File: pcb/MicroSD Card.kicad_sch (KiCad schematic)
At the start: 2 parts, among them J4 Micro_SD_Card

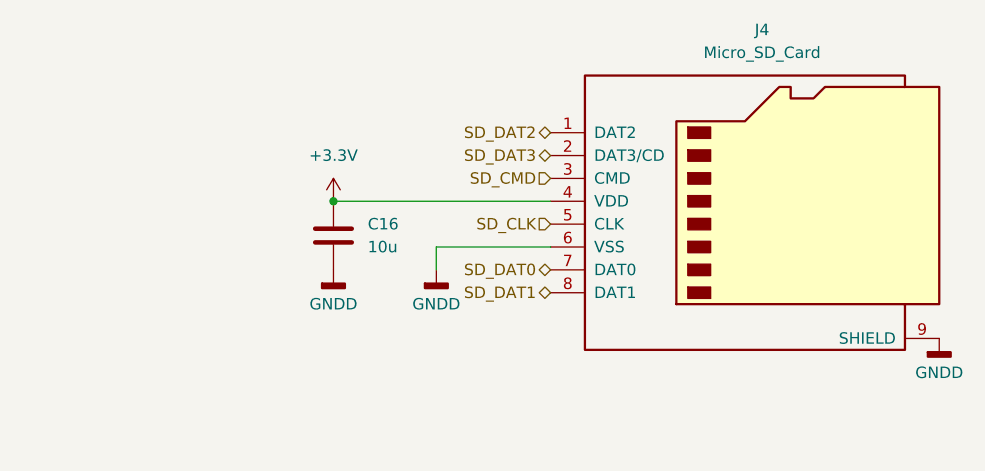
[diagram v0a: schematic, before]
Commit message: Updated Control Module Test bed schematics
Added Test points for Pyro controllers, Micro SD, and USB-C

Connected VDDUSB to 3.3V and not Vusb
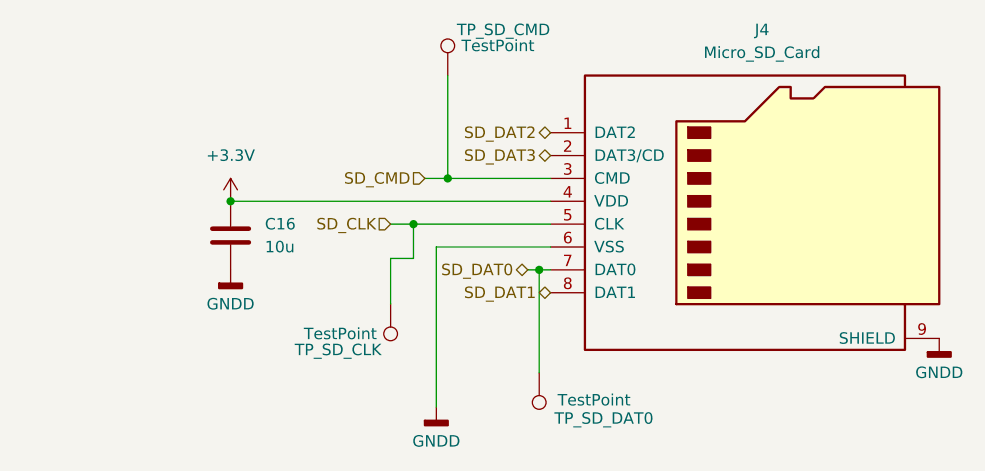
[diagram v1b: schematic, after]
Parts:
- added TP_SD_CLK, TP_SD_CMD, TP_SD_DAT0: TestPoint, TestPoint:TestPoint_Loop_D2.54mm_Drill1.5mm_Beaded, symbol Connector:TestPoint
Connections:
- net SD_CLK: now also TP_SD_CLK.1
- net SD_CMD: now also TP_SD_CMD.1
- net SD_DAT0: now also TP_SD_DAT0.1
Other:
- moved on the sheet: C16

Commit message: Added more testpoints
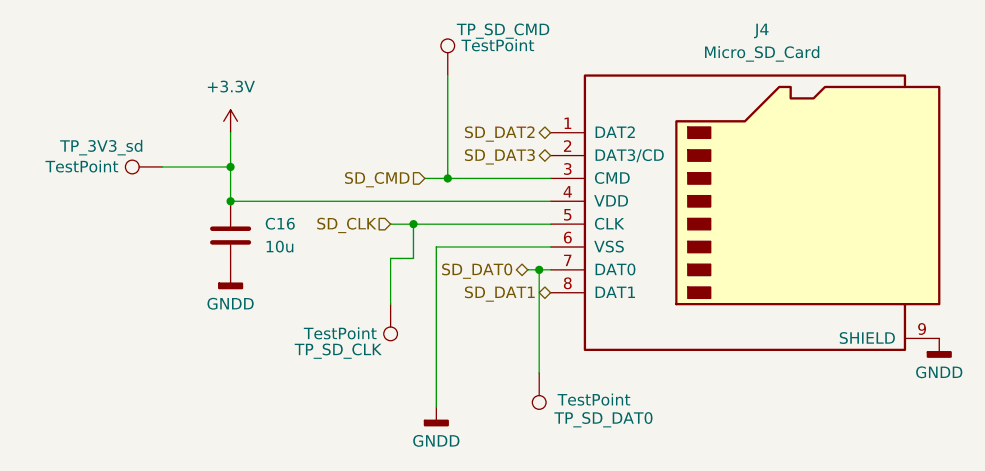
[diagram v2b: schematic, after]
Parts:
- added TP_3V3_sd: TestPoint, TestPoint:TestPoint_Loop_D2.54mm_Drill1.5mm_Beaded, symbol Connector:TestPoint
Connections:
- net +3.3V: now also TP_3V3_sd.1
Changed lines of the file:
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@@
+	)
+	(junction
+		(at 90.17 83.82)
+		(diameter 0)
+		(color 0 0 0 0)
 	)
 	(junction
@@
 	(wire
 		(pts
+			(xy 82.55 83.82) (xy 90.17 83.82)
+		)
+		(stroke
+			(width 0)
+			(type default)
+		)
+	)
+	(wire
+		(pts
 			(xy 110.49 90.17) (xy 125.73 90.17)
 		)
@@
 		(pts
 			(xy 124.46 95.25) (xy 124.46 106.68)
+		)
+		(stroke
+			(width 0)
+			(type default)
+		)
+	)
+	(wire
+		(pts
+			(xy 90.17 83.82) (xy 90.17 87.63)
+		)
+		(stroke
+			(width 0)
+			(type default)
+		)
+	)
+	(wire
+		(pts
+			(xy 90.17 80.01) (xy 90.17 83.82)
 		)
 		(stroke
@@
 	(symbol
 		(lib_id "power:+3.3V")
-		(at 90.17 87.63 0)
+		(at 90.17 80.01 0)
 		(unit 1)
 		(exclude_from_sim no)
@@
 		(fields_autoplaced yes)
 		(property "Reference" "#PWR050"
-			(at 90.17 91.44 0)
+			(at 90.17 83.82 0)
 			(effects
 				(font
@@
 		)
 		(property "Value" "+3.3V"
-			(at 90.17 82.55 0)
+			(at 90.17 74.93 0)
 			(effects
 				(font
@@
 		)
 		(property "Footprint" ""
-			(at 90.17 87.63 0)
+			(at 90.17 80.01 0)
 			(effects
 				(font
@@
 		)
 		(property "Datasheet" ""
-			(at 90.17 87.63 0)
+			(at 90.17 80.01 0)
 			(effects
 				(font
@@
 		)
 		(property "Description" "Power symbol creates a global label with name \"+3.3V\""
-			(at 90.17 87.63 0)
+			(at 90.17 80.01 0)
 			(effects
 				(font
@@
 					(unit 1)
 				)
+			)
+		)
+	)
+	(symbol
+		(lib_id "Connector:TestPoint")
+		(at 82.55 83.82 90)
+		(unit 1)
+		(exclude_from_sim no)
+		(in_bom yes)
+		(on_board yes)
+		(dnp no)
+		(property "Reference" "TP_3V3_sd"
+			(at 80.518 81.534 90)
+			(effects
+				(font
+					(size 1.27 1.27)
+				)
+				(justify left)
+			)
+		)
+		(property "Value" "TestPoint"
+			(at 77.724 83.82 90)
+			(effects
+				(font
+					(size 1.27 1.27)
+				)
+				(justify left)
+			)
+		)
+		(property "Footprint" "TestPoint:TestPoint_Loop_D2.54mm_Drill1.5mm_Beaded"
+			(at 82.55 78.74 0)
+			(effects
+				(font
+					(size 1.27 1.27)
+				)
+				(hide yes)
+			)
+		)
+		(property "Datasheet" "https://www.keyelco.com/userAssets/file/M65p56.pdf"
+			(at 82.55 78.74 0)
+			(effects
+				(font
+					(size 1.27 1.27)
+				)
+				(hide yes)
+			)
+		)
+		(property "Description" "test point"
+			(at 82.55 83.82 0)
+			(effects
+				(font
+					(size 1.27 1.27)
+				)
+				(hide yes)
+			)
+		)
+		(property "Purchase" "https://www.digikey.com/en/products/detail/keystone-electronics/5000/255326"
+			(at 82.55 83.82 0)
+			(effects
+				(font
+					(size 1.27 1.27)
+				)
+				(hide yes)
+			)
+		)
+		(pin "1"
+		)
+		(instances
+			(project "control-module"
+				(path "/ba7b4294-8d75-4b9e-892f-fb52727887ec/02a5c5f6-b4e2-435d-aca7-a6d22478aa51"
+					(reference "TP_3V3_sd")
+					(unit 1)
+				)

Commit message: Updated Schematics
Completed Schematics for Test Bed, updated pcb
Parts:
- C14: renamed from C16; value 10u -> 10uF
- renumbered TP_3V3_sd to TP_3V3_sd1, TP_SD_CLK to TP_SD_CLK1, TP_SD_CMD to TP_SD_CMD1, TP_SD_DAT0 to TP_SD_DAT1
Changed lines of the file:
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@@
 		(dnp no)
 		(fields_autoplaced yes)
-		(property "Reference" "#PWR052"
+		(property "Reference" "#PWR062"
 			(at 113.03 116.84 0)
 			(effects
@@
 			(project ""
 				(path "/ba7b4294-8d75-4b9e-892f-fb52727887ec/02a5c5f6-b4e2-435d-aca7-a6d22478aa51"
-					(reference "#PWR052")
+					(reference "#PWR062")
 					(unit 1)
 				)
@@
 		(on_board yes)
 		(dnp no)
-		(property "Reference" "TP_SD_CMD"
+		(property "Reference" "TP_SD_CMD1"
 			(at 115.316 68.58 0)
 			(effects
@@
 			(project "control-module"
 				(path "/ba7b4294-8d75-4b9e-892f-fb52727887ec/02a5c5f6-b4e2-435d-aca7-a6d22478aa51"
-					(reference "TP_SD_CMD")
+					(reference "TP_SD_CMD1")
 					(unit 1)
 				)
@@
 		(on_board yes)
 		(dnp no)
-		(property "Reference" "TP_SD_DAT0"
+		(property "Reference" "TP_SD_DAT1"
 			(at 137.16 111.76 0)
 			(effects
@@
 			(project "control-module"
 				(path "/ba7b4294-8d75-4b9e-892f-fb52727887ec/02a5c5f6-b4e2-435d-aca7-a6d22478aa51"
-					(reference "TP_SD_DAT0")
+					(reference "TP_SD_DAT1")
 					(unit 1)
 				)
@@
 		(dnp no)
 		(fields_autoplaced yes)
-		(property "Reference" "#PWR050"
+		(property "Reference" "#PWR060"
 			(at 90.17 83.82 0)
 			(effects
@@
 			(project ""
 				(path "/ba7b4294-8d75-4b9e-892f-fb52727887ec/02a5c5f6-b4e2-435d-aca7-a6d22478aa51"
-					(reference "#PWR050")
+					(reference "#PWR060")
 					(unit 1)
 				)
@@
 		(dnp no)
 		(fields_autoplaced yes)
-		(property "Reference" "#PWR051"
+		(property "Reference" "#PWR061"
 			(at 90.17 101.6 0)
 			(effects
@@
 			(project ""
 				(path "/ba7b4294-8d75-4b9e-892f-fb52727887ec/02a5c5f6-b4e2-435d-aca7-a6d22478aa51"
-					(reference "#PWR051")
+					(reference "#PWR061")
 					(unit 1)
 				)
@@
 		(on_board yes)
 		(dnp no)
-		(property "Reference" "TP_SD_CLK"
+		(property "Reference" "TP_SD_CLK1"
 			(at 106.934 104.14 0)
 			(effects
@@
 			(project "control-module"
 				(path "/ba7b4294-8d75-4b9e-892f-fb52727887ec/02a5c5f6-b4e2-435d-aca7-a6d22478aa51"
-					(reference "TP_SD_CLK")
+					(reference "TP_SD_CLK1")
 					(unit 1)
 				)
@@
 		(dnp no)
 		(fields_autoplaced yes)
-		(property "Reference" "#PWR053"
+		(property "Reference" "#PWR063"
 			(at 168.91 109.22 0)
 			(effects
@@
 			(project ""
 				(path "/ba7b4294-8d75-4b9e-892f-fb52727887ec/02a5c5f6-b4e2-435d-aca7-a6d22478aa51"
-					(reference "#PWR053")
+					(reference "#PWR063")
 					(unit 1)
 				)
@@
 		(dnp no)
 		(fields_autoplaced yes)
-		(property "Reference" "C16"
+		(property "Reference" "C14"
 			(at 93.98 90.1699 0)
 			(effects
@@
 			)
 		)
-		(property "Value" "10u"
+		(property "Value" "10uF"
 			(at 93.98 92.7099 0)
 			(effects
@@
 			(project ""
 				(path "/ba7b4294-8d75-4b9e-892f-fb52727887ec/02a5c5f6-b4e2-435d-aca7-a6d22478aa51"
-					(reference "C16")
+					(reference "C14")
 					(unit 1)
 				)
@@
 		(on_board yes)
 		(dnp no)
-		(property "Reference" "TP_3V3_sd"
+		(property "Reference" "TP_3V3_sd1"
 			(at 80.518 81.534 90)
 			(effects
@@
 			(project "control-module"
 				(path "/ba7b4294-8d75-4b9e-892f-fb52727887ec/02a5c5f6-b4e2-435d-aca7-a6d22478aa51"
-					(reference "TP_3V3_sd")
-					(unit 1)
-				)
+					(reference "TP_3V3_sd1")
+					(unit 1)
+				)

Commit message: Pre-fab update
Pre fab update
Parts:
- renumbered TP_3V3_sd1 to 3V3_sd1, TP_SD_CLK1 to SD_CLK1, TP_SD_CMD1 to SD_CMD1, TP_SD_DAT1 to SD_DAT1
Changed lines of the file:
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@@
 		(on_board yes)
 		(dnp no)
-		(property "Reference" "TP_SD_CMD1"
+		(property "Reference" "SD_CMD1"
 			(at 115.316 68.58 0)
 			(effects
@@
 			)
 		)
+		(property "Sim.Device" ""
+			(at 114.3 73.66 0)
+			(effects
+				(font
+					(size 1.27 1.27)
+				)
+				(hide yes)
+			)
+		)
 		(pin "1"
 		)
@@
 			(project "control-module"
 				(path "/ba7b4294-8d75-4b9e-892f-fb52727887ec/02a5c5f6-b4e2-435d-aca7-a6d22478aa51"
-					(reference "TP_SD_CMD1")
+					(reference "SD_CMD1")
 					(unit 1)
 				)
@@
 		(on_board yes)
 		(dnp no)
-		(property "Reference" "TP_SD_DAT1"
+		(property "Reference" "SD_DAT1"
 			(at 137.16 111.76 0)
 			(effects
@@
 			)
 		)
+		(property "Sim.Device" ""
+			(at 124.46 106.68 0)
+			(effects
+				(font
+					(size 1.27 1.27)
+				)
+				(hide yes)
+			)
+		)
 		(pin "1"
 		)
@@
 			(project "control-module"
 				(path "/ba7b4294-8d75-4b9e-892f-fb52727887ec/02a5c5f6-b4e2-435d-aca7-a6d22478aa51"
-					(reference "TP_SD_DAT1")
+					(reference "SD_DAT1")
 					(unit 1)
 				)
@@
 		(on_board yes)
 		(dnp no)
-		(property "Reference" "TP_SD_CLK1"
+		(property "Reference" "SD_CLK1"
 			(at 106.934 104.14 0)
 			(effects
@@
 			)
 		)
+		(property "Sim.Device" ""
+			(at 107.95 99.06 0)
+			(effects
+				(font
+					(size 1.27 1.27)
+				)
+				(hide yes)
+			)
+		)
 		(pin "1"
 		)
@@
 			(project "control-module"
 				(path "/ba7b4294-8d75-4b9e-892f-fb52727887ec/02a5c5f6-b4e2-435d-aca7-a6d22478aa51"
-					(reference "TP_SD_CLK1")
+					(reference "SD_CLK1")
 					(unit 1)
 				)
@@
 			)
 		)
+		(property "Sim.Device" ""
+			(at 90.17 91.44 0)
+			(effects
+				(font
+					(size 1.27 1.27)
+				)
+				(hide yes)
+			)
+		)
 		(pin "2"
 		)
@@
 			)
 		)
+		(property "Sim.Device" ""
+			(at 148.59 87.63 0)
+			(effects
+				(font
+					(size 1.27 1.27)
+				)
+				(hide yes)
+			)
+		)
 		(pin "8"
 		)
@@
 		(on_board yes)
 		(dnp no)
-		(property "Reference" "TP_3V3_sd1"
+		(property "Reference" "3V3_sd1"
 			(at 80.518 81.534 90)
 			(effects
@@
 			)
 		)
+		(property "Sim.Device" ""
+			(at 82.55 83.82 90)
+			(effects
+				(font
+					(size 1.27 1.27)
+				)
+				(hide yes)
+			)
+		)
 		(pin "1"
 		)
@@
 			(project "control-module"
 				(path "/ba7b4294-8d75-4b9e-892f-fb52727887ec/02a5c5f6-b4e2-435d-aca7-a6d22478aa51"
-					(reference "TP_3V3_sd1")
-					(unit 1)
-				)
+					(reference "3V3_sd1")
+					(unit 1)
+				)
